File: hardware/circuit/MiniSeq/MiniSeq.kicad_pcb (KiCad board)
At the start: 2 copper layers, 170 x 128.5 mm, 97 parts, among them J1 Conn_01x10_Pin, SW1 SMTS-102, SW11 RESET_BTN, SW2 SMTS-102, SW3 SMTS-102, SW4 SMTS-102, SW5 SMTS-102, SW6 SMTS-102, SW7 SMTS-102, SW8 SMTS-102, SW9 CLOCK_BTN, U1 4017, U2 TL072, U3 TL074, U4 L7809CD2T-TR

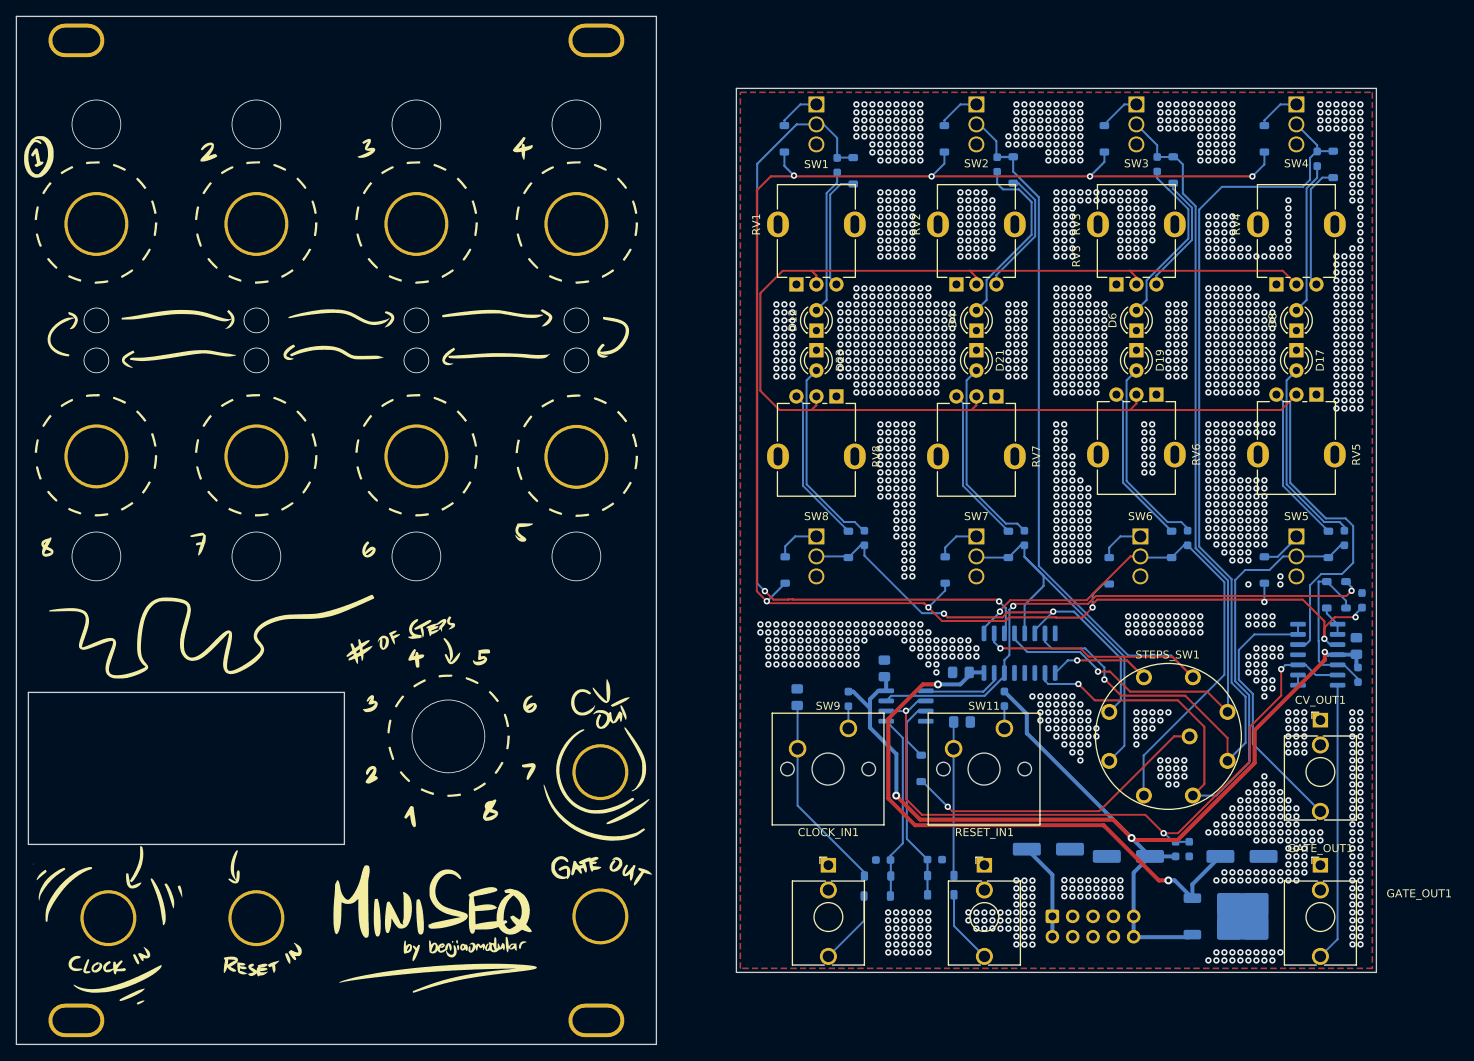
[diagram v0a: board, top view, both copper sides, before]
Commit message: Added copper fills to panel
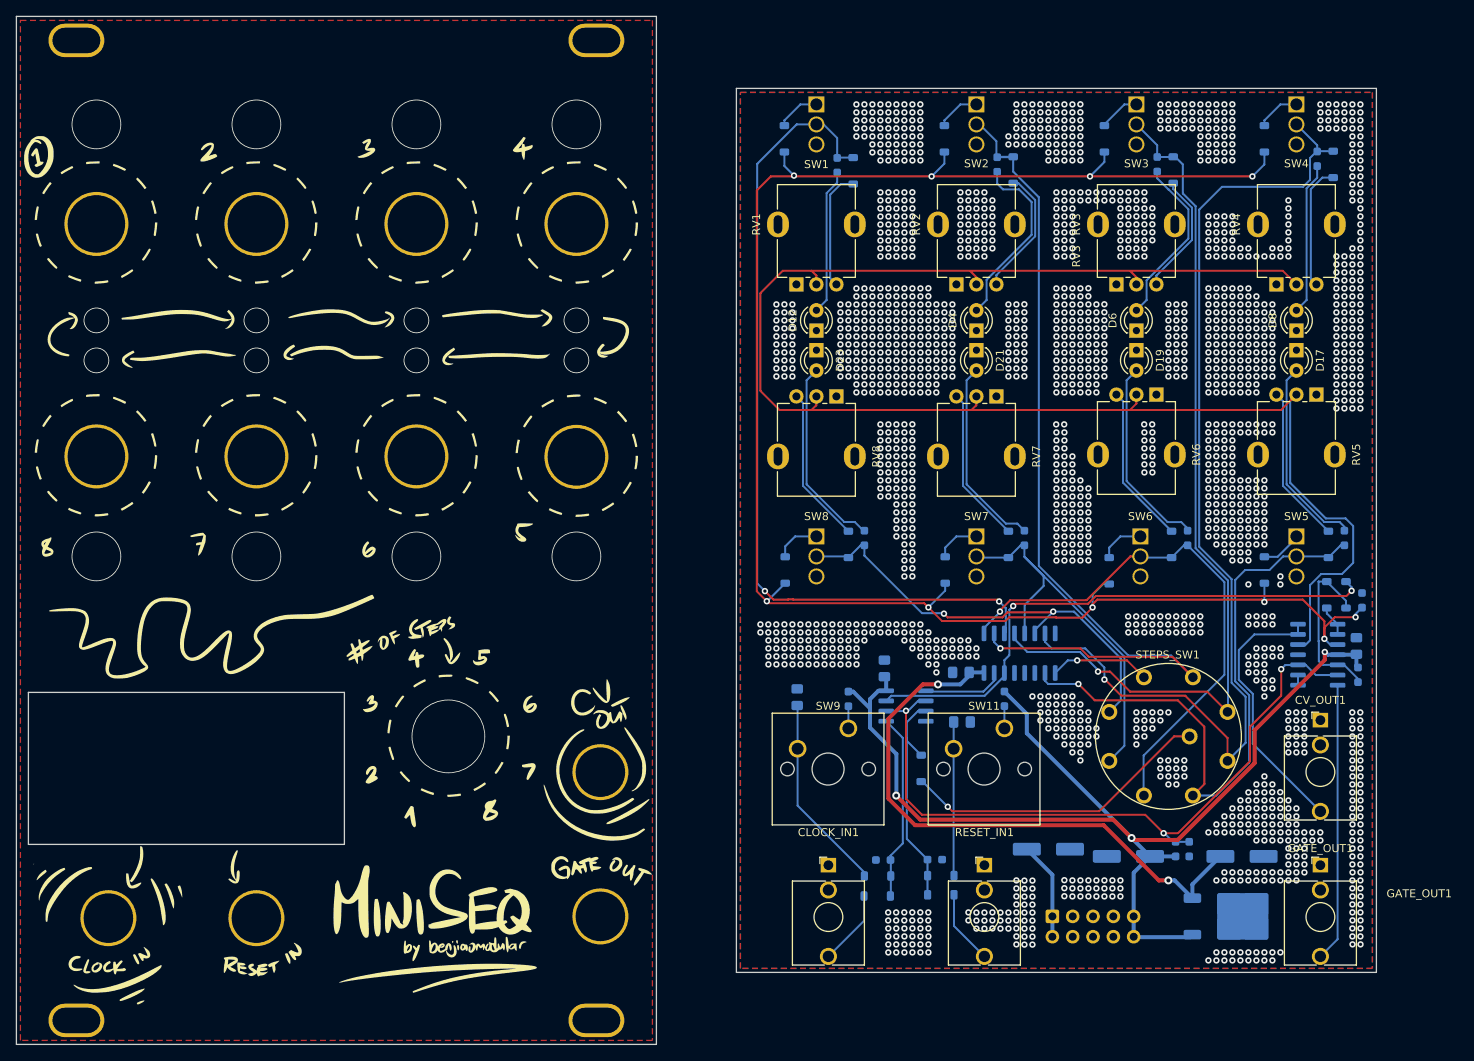
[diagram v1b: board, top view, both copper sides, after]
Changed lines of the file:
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@@
+		(layer "F.Cu")
+		(hatch edge 0.5)
+		(priority 2)
+		(connect_pads
+			(clearance 0.508)
+		)
+		(min_thickness 0.25)
+		(filled_areas_thickness no)
+		(fill yes
+			(thermal_gap 0.5)
+			(thermal_bridge_width 0.5)
+		)
+		(polygon
+			(pts
+				(xy 50.5 30.5) (xy 129.5 30.5) (xy 129.5 158) (xy 50.5 158)
+			)
+		)
+	)
+	(zone
+		(net 2)
+		(net_name "GND")
 		(layer "F.Cu")
 		(hatch edge 0.5)

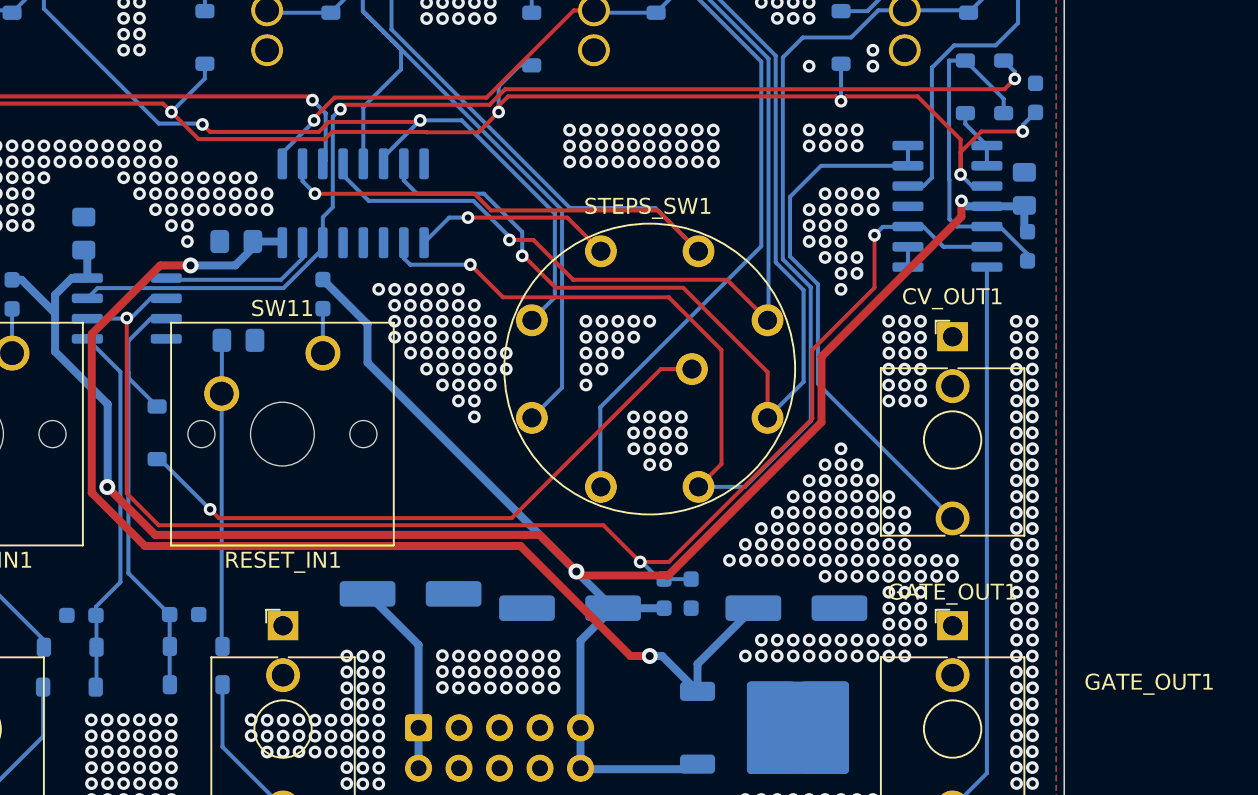
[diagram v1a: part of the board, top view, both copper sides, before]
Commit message: Updated PCBs for v0.1
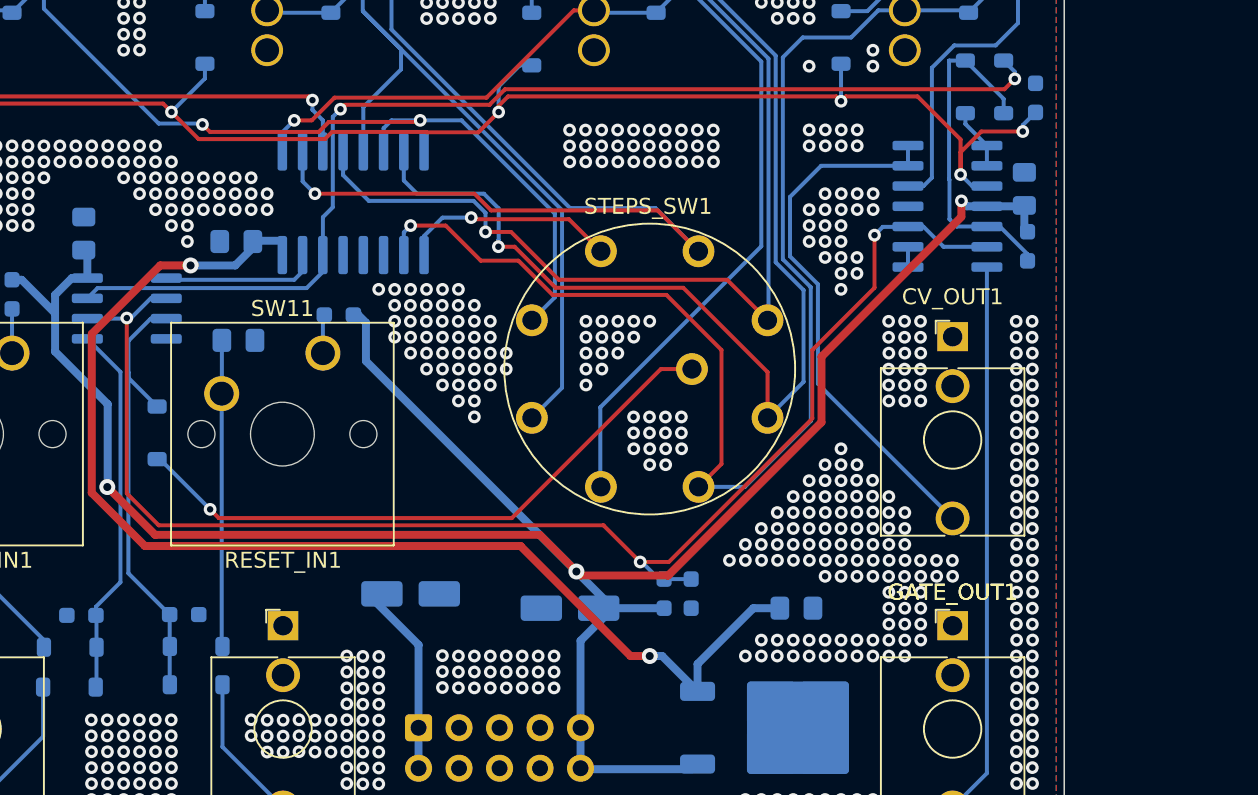
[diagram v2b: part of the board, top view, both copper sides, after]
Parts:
- C4, C5: footprint Capacitor_SMD:CP_Elec_6.3x4.5 -> Capacitor_SMD:CP_Elec_4x3.9
- C6: footprint Capacitor_SMD:CP_Elec_6.3x4.5 -> Capacitor_SMD:C_0805_2012Metric_Pad1.18x1.45mm_HandSolder
- U1: footprint Package_SO:SOIC-16_3.9x9.9mm_P1.27mm -> Package_SO:SOIC-16W_5.3x10.2mm_P1.27mm
- moved R9 1.64 mm to (174.5, 116.6), turned to 0 degrees
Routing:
- net +12V: track 145.5 -> 142.7 mm
- net +9V: track 74.3 -> 76.0 mm
- net /STEP5: track 80.3 -> 82.0 mm
- net /STEP4: track 130.7 -> 132.0 mm
- net /STEP8: track 56.9 -> 58.0 mm
- net /STEP1: track 105.3 -> 104.4 mm
- net /CLOCK: track 69.8 -> 70.6 mm
- net /STEP7: track 51.1 -> 50.4 mm
- net /STEP6: track 68.0 -> 68.7 mm
- net /STEP3: track 110.8 -> 111.4 mm
